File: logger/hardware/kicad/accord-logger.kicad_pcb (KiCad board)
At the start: 2 copper layers, 120 x 80 mm, 31 parts, among them J1 Board connector 14-way, J5 SD breakout 6-way, Q5 IPD50P04P4L-11, Q6 MMBT3904, Q7 MMBT3904, U1 RaspberryPi_Pico_W, U6 LM2678T-5.0

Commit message: layout: power block placed, C8 at the SD header, first 22 tracks
Owner's layout in progress: the buck, entry protection, power switch and
hold transistors placed (17 parts on the board outline, others still
being positioned), C8 at J5, and the first 22 track segments.

Checked before commit: every footprint and pad net matches the
schematic; no extra fields visible on silkscreen.

Committed on the owner's behalf.
Claude-Session-ID: 42dd0e33-28b5-4936-847e-9c2e1d2488fa
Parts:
- C12, C9: moved to B.Cu
- moved Q5 253.8 mm to (172.7, 111.8), turned to 90 degrees
- moved C8 249.4 mm to (119.4, 72.4)
- moved U6 219.3 mm to (173.5, 123.1), turned to -90 degrees
- moved C14 215.2 mm to (160.7, 114.4), turned to -90 degrees
- moved Q6 213.4 mm to (164.5, 99.1)
- moved D116 211.6 mm to (142.0, 81.9)
- moved C12 191.3 mm to (170.8, 124.5), turned to -90 degrees
- moved L1 189.0 mm to (160.6, 129.4), turned to 180 degrees
- moved C13 182.8 mm to (179.1, 134.0)
- moved C10 176.0 mm to (186.7, 127.6)
- moved D115 165.8 mm to (167.0, 129.4), turned to 90 degrees
- moved C9 162.1 mm to (192.6, 121.3)
- moved Q7 157.8 mm to (220.0, 102.6)
- moved D112 148.1 mm to (185.6, 117.5), turned to 180 degrees
- moved C11 143.0 mm to (233.2, 95.9)
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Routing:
- net /VSYS: track 0.00 -> 57.2 mm, vias 0 -> 1
- net /SD_MISO: track 0.00 -> 46.4 mm
- net /SD_CS: track 0.00 -> 42.1 mm
- net /B5: track 0.00 -> 38.1 mm
- net /SD_SCK: track 0.00 -> 36.3 mm
- net /SD_MOSI: track 0.00 -> 32.4 mm

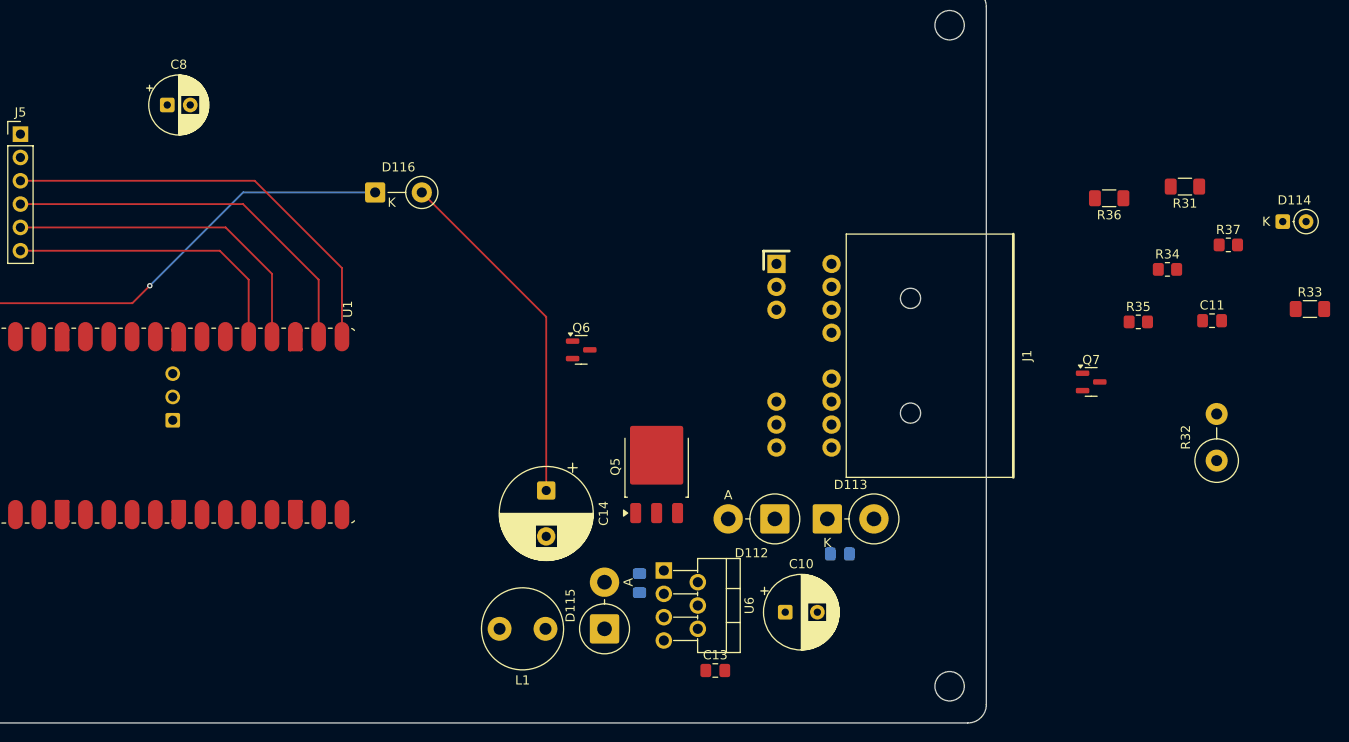
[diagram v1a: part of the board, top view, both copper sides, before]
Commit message: layout: power block placed on the board
Owner's layout: all 27 power-block, Pico, SD and J1 parts on the board,
with the D-THT-13 through-hole footprints applied from the schematic; 23
track segments so far.

Review at this commit (DRC on a scratch copy, schematic parity 0):
- courtyard overlap R32 / C14, to fix;
- the Pico's antenna end sits mid-board (keepout x 43-61 mm), USB at the
  left edge; Pico guidance wants the antenna at an edge;
- buck loop distances (CIN-VIN 11, CIN- to GND 14, catch diode to SW 9,
  catch anode to CIN- 25 mm) match the in-service keyless layout within
  ~2 mm; tighter would still help;
- U1 RF-keepout and J1 silk-at-edge items come from the footprints.

Committed on the owner's behalf.
Claude-Session-ID: 42dd0e33-28b5-4936-847e-9c2e1d2488fa
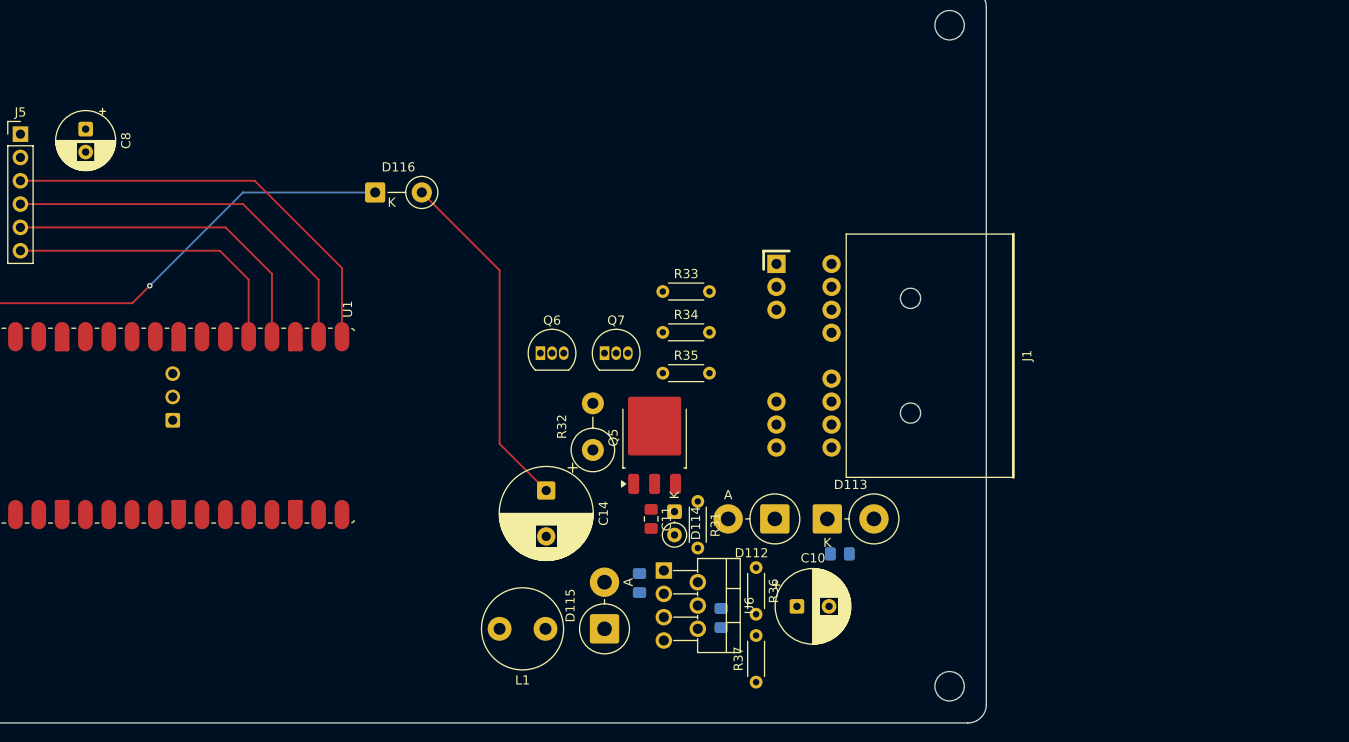
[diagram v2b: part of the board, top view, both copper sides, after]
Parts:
- C13: moved to B.Cu
- Q6, Q7: value MMBT3904 -> 2N3904; footprint Package_TO_SOT_SMD:SOT-23 -> Package_TO_SOT_THT:TO-92_Inline
- R31, R33, R36: footprint Resistor_SMD:R_1206_3216Metric_Pad1.30x1.75mm_HandSolder -> Resistor_THT:R_Axial_DIN0204_L3.6mm_D1.6mm_P5.08mm_Horizontal
- R34, R35, R37: footprint Resistor_SMD:R_0805_2012Metric_Pad1.20x1.40mm_HandSolder -> Resistor_THT:R_Axial_DIN0204_L3.6mm_D1.6mm_P5.08mm_Horizontal
- moved D114 73.4 mm to (174.6, 116.7), turned to -90 degrees
- moved R33 70.5 mm to (173.4, 92.7)
- moved R37 70.1 mm to (183.5, 135.3), turned to 90 degrees
- moved R32 68.0 mm to (165.7, 110.0)
- moved C11 64.8 mm to (172.1, 117.5), turned to -90 degrees
- moved R31 63.2 mm to (177.2, 115.6), turned to -90 degrees
- moved R36 55.7 mm to (183.5, 122.8), turned to -90 degrees
- moved R34 55.4 mm to (173.4, 97.2)
- moved Q7 53.1 mm to (167.0, 99.4)
- moved R35 52.1 mm to (173.4, 101.6)
- moved C8 9.27 mm to (110.5, 75.0), turned to -90 degrees
- moved C13 5.75 mm to (179.7, 128.3), turned to 90 degrees
- moved Q6 4.46 mm to (160.0, 99.4)
- moved Q5 3.18 mm to (172.5, 108.6)
- moved C10 1.42 mm to (188.0, 127.0)
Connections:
- Q6 pad 1: /IGN_B -> /PGND
- Q6 pad 2: /PGND -> /IGN_B
- Q7 pad 1: /HOLD_B -> /PGND
- Q7 pad 2: /PGND -> /HOLD_B
